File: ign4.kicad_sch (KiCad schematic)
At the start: 13 parts, among them U44 MIC4427, U45 MIC4427

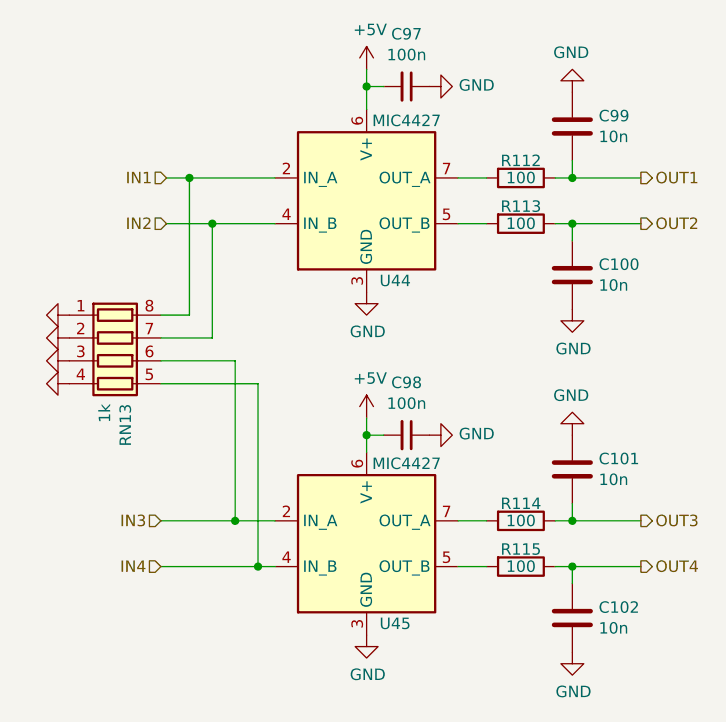
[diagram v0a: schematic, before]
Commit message: Published 1.5 gerbs, bom, cpl and pdf
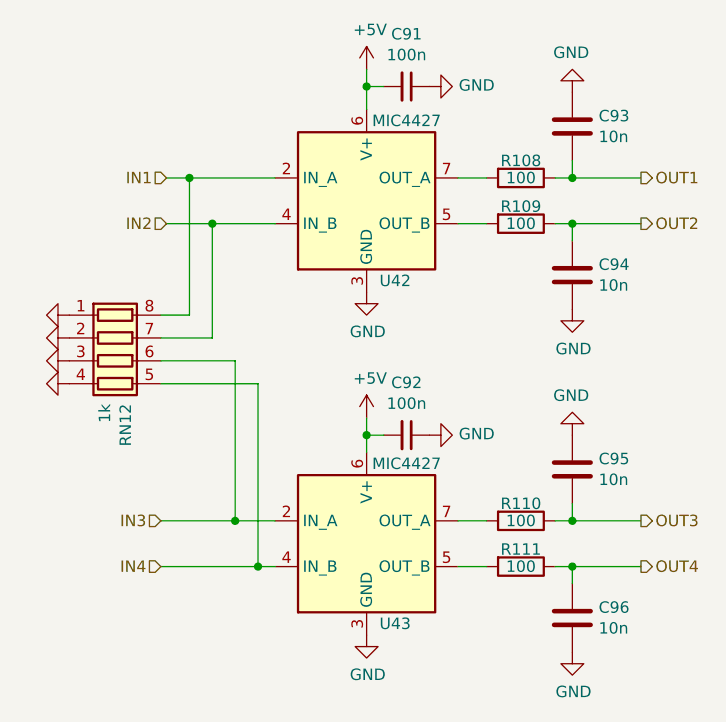
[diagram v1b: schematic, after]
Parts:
- renumbered C97 to C91, C98 to C92, C99 to C93, C100 to C94, C101 to C95, C102 to C96, R112 to R108, R113 to R109, R114 to R110, R115 to R111, RN13 to RN12, U44 to U42, U45 to U43

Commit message: make hardware updates: - fix erc/drc errors - switch to VNLD5090 - switch to SOIC8 ignition drivers - BOM deduplication of similar parts
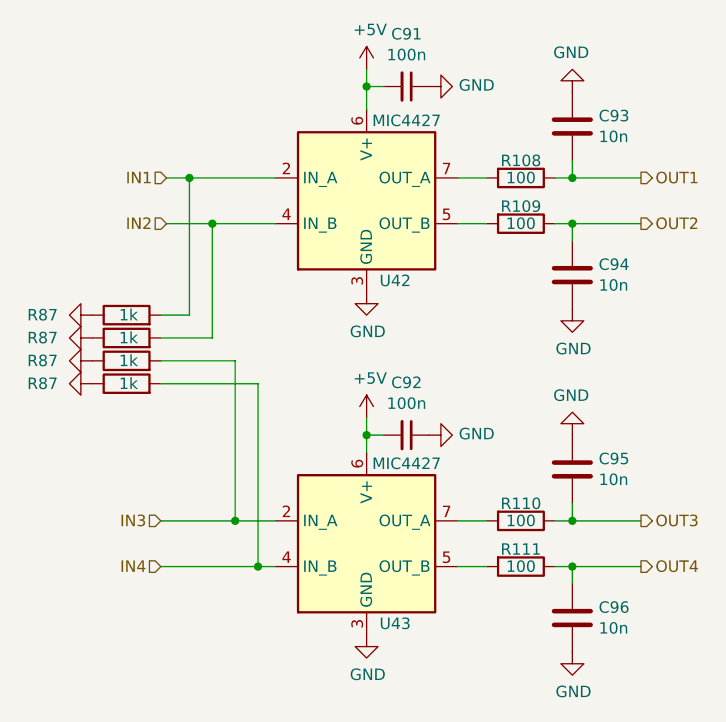
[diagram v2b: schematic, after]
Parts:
- removed RN12: 1k, Resistor_SMD:R_Array_Convex_4x0603, symbol Device:R_Pack04
- added R87 (x4): 1k, Resistor_SMD:R_0402_1005Metric, symbol Device:R
- U42, U43: footprint Package_SO:MSOP-8_3x3mm_P0.65mm -> Package_SO:SO-8_3.9x4.9mm_P1.27mm; LCSC C20551 -> C171845
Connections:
- net GND: now also R87.1, R87.1, R87.1, R87.1
- net IN1: now also R87.2
- net IN2: now also R87.2
- net IN3: now also R87.2
- net IN4: now also R87.2
